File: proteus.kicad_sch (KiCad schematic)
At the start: 30 parts, among them J1 Conn_01x01, J13 Conn_01x03, J15 Sicma_56, J2 Conn_01x01, J3 Conn_01x01, J4 Conn_01x03, J5 Conn_01x05, J6 Conn_02x04_Counter_Clockwise, J9 Conn_01x04

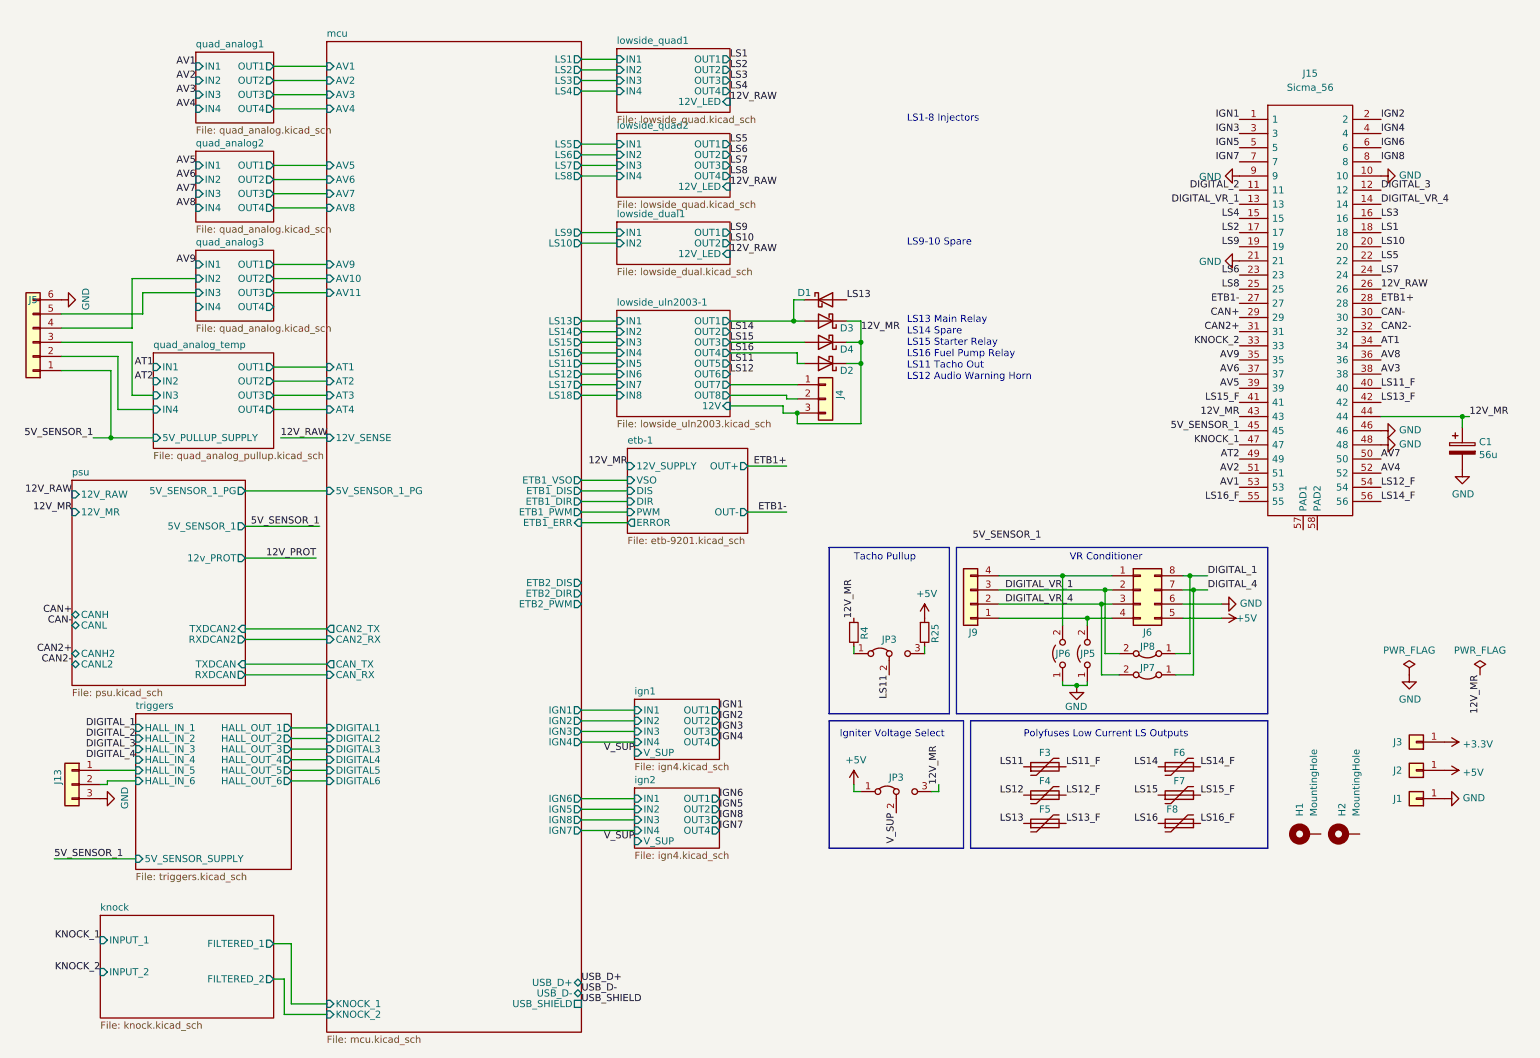
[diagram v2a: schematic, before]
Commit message: Add Stepper, fix Connector, add Testpoints, several changes
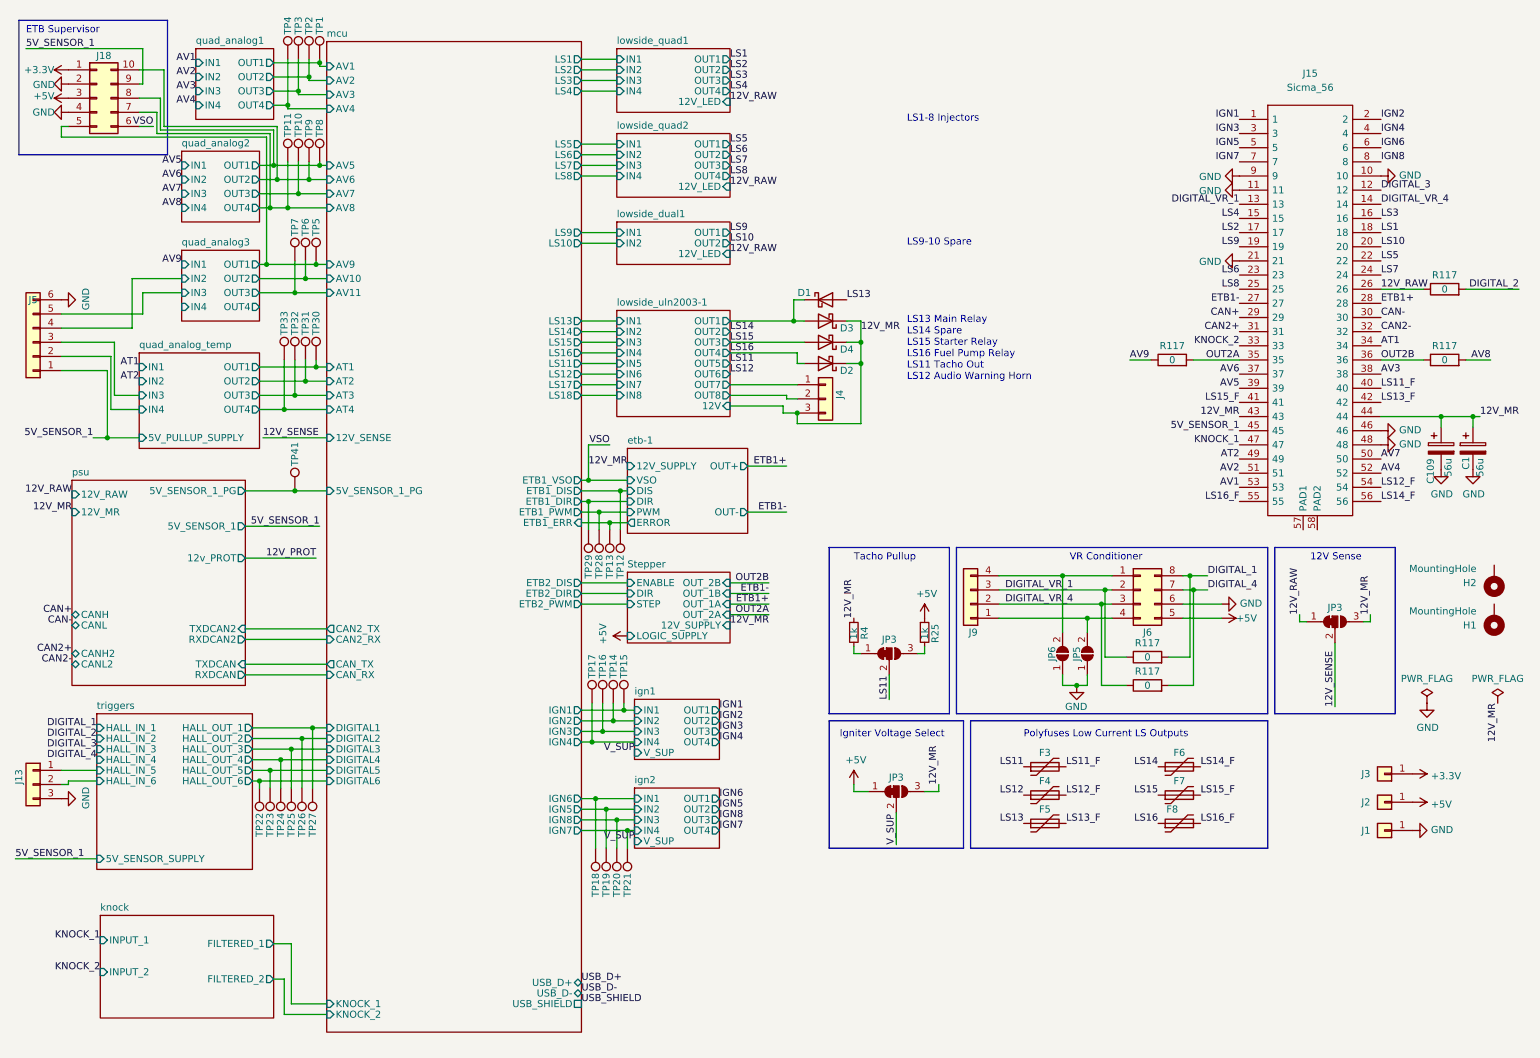
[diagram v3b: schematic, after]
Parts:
- removed JP7, JP8: Jumper_2_Bridged, Jumper:SolderJumper-2_P1.3mm_Bridged_RoundedPad1.0x1.5mm, symbol Jumper:Jumper_2_Bridged
- added C109: 56u, Capacitor_THT:CP_Radial_D8.0mm_P3.50mm, symbol proteus-rescue:CP-Device
- added J18: Conn_02x04_Counter_Clockwise, Connector_PinHeader_2.54mm:PinHeader_2x05_P2.54mm_Vertical, symbol Connector_Generic:Conn_02x05_Counter_Clockwise
- added JP3: Jumper_3_Bridged12, Jumper:SolderJumper-3_P1.3mm_Bridged12_RoundedPad1.0x1.5mm, symbol Jumper:SolderJumper_3_Bridged12
- added R117 (x5): 0, Resistor_SMD:R_0402_1005Metric, symbol Device:R
- added TP1, TP10, TP11, TP12, TP13, TP14, TP15, TP16, TP17, TP18, TP19, TP2, TP20, TP21, TP22, TP23, TP24, TP25, TP26, TP27, TP28, TP29, TP3, TP30, TP31, TP32, TP33, TP4, TP41, TP5, TP6, TP7, TP8, TP9: TestPoint, TestPoint:TestPoint_Pad_D1.0mm, symbol Connector:TestPoint
- D1, D2, D3, D4: LCSC C15874 -> C14996
- H1, H2, J1, J13, J15, J2, J3, J4, J5, J6, J9: now left out of the parts list
- JP3: symbol Jumper:Jumper_3_Bridged12 -> Jumper:SolderJumper_3_Bridged12; now left out of the parts list
- JP5, JP6: symbol Jumper:Jumper_2_Open -> Jumper:SolderJumper_2_Open; now left out of the parts list
- R25, R4: value R_Small -> 1k; footprint Resistor_SMD:R_0805_2012Metric -> Resistor_SMD:R_0402_1005Metric; LCSC (none) -> C106235
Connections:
- net +3V3: now also J18.1 (Pin_1)
- net +5V: now also J18.3 (Pin_3)
- net 12V_MR: now also C109.1, JP3.3 (B)
- net 12V_RAW: now also JP3.1 (A), R117.1
- net 5V_SENSOR_1: now also J18.9 (Pin_9)
- net AV8: now also R117.2; no longer J15.36
- net AV9: now also R117.1; no longer J15.35
- net DIGITAL_1: now also R117.2
- net DIGITAL_2: now also R117.2; no longer J15.11
- net DIGITAL_4: now also R117.2
- net DIGITAL_VR_1: now also R117.1
- net DIGITAL_VR_4: now also R117.1
- net GND: now also J15.11, C109.2, J18.2 (Pin_2), J18.4 (Pin_4)
- net etb-1/DIR: now also TP29.1
- net etb-1/DIS: now also TP12.1
- net etb-1/ERROR: now also TP13.1
- net etb-1/PWM: now also TP28.1
- net ign1/IN1: now also TP15.1
- net ign1/IN2: now also TP14.1
- net ign1/IN3: now also TP16.1
- net ign1/IN4: now also TP17.1
- net ign2/IN1: now also TP18.1
- net ign2/IN2: now also TP19.1
- net ign2/IN3: now also TP20.1
- net ign2/IN4: now also TP21.1
- net mcu/5V_SENSOR_1_PG: now also TP41.1
- net mcu/AT1: now also TP30.1
- net mcu/AT2: now also TP31.1
- net mcu/AT3: now also TP32.1
- net mcu/AT4: now also TP33.1
- net mcu/AV1: now also TP1.1
- net mcu/AV10: now also TP6.1
- net mcu/AV11: now also TP7.1
- net mcu/AV2: now also TP2.1
- net mcu/AV3: now also TP3.1
- net mcu/AV4: now also TP4.1
- net mcu/AV5: now also J18.8 (Pin_8), TP8.1
- net mcu/AV6: now also J18.10 (Pin_10), TP9.1
- net mcu/AV7: now also TP10.1
- net mcu/AV8: now also J18.7 (Pin_7), TP11.1
- net mcu/AV9: now also J18.5 (Pin_5), TP5.1
- net mcu/DIGITAL1: now also TP27.1
- net mcu/DIGITAL2: now also TP26.1
- net mcu/DIGITAL3: now also TP25.1
- net mcu/DIGITAL4: now also TP24.1
- net mcu/DIGITAL5: now also TP23.1
- net mcu/DIGITAL6: now also TP22.1
- new net 12V_SENSE: JP3.2 (C)
- new net OUT2A: J15.35, R117.2
- new net OUT2B: J15.36, R117.1
- new net VSO: J18.6 (Pin_6)
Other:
- added sheet Stepper (stepper.kicad_sch)
- note added: "12V Sense"
- note added: "ETB Supervisor"
- moved on the sheet: C1, H1, H2, J1, J13, J2, J3

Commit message: Production optimizations, voltage superv, etb sv conn
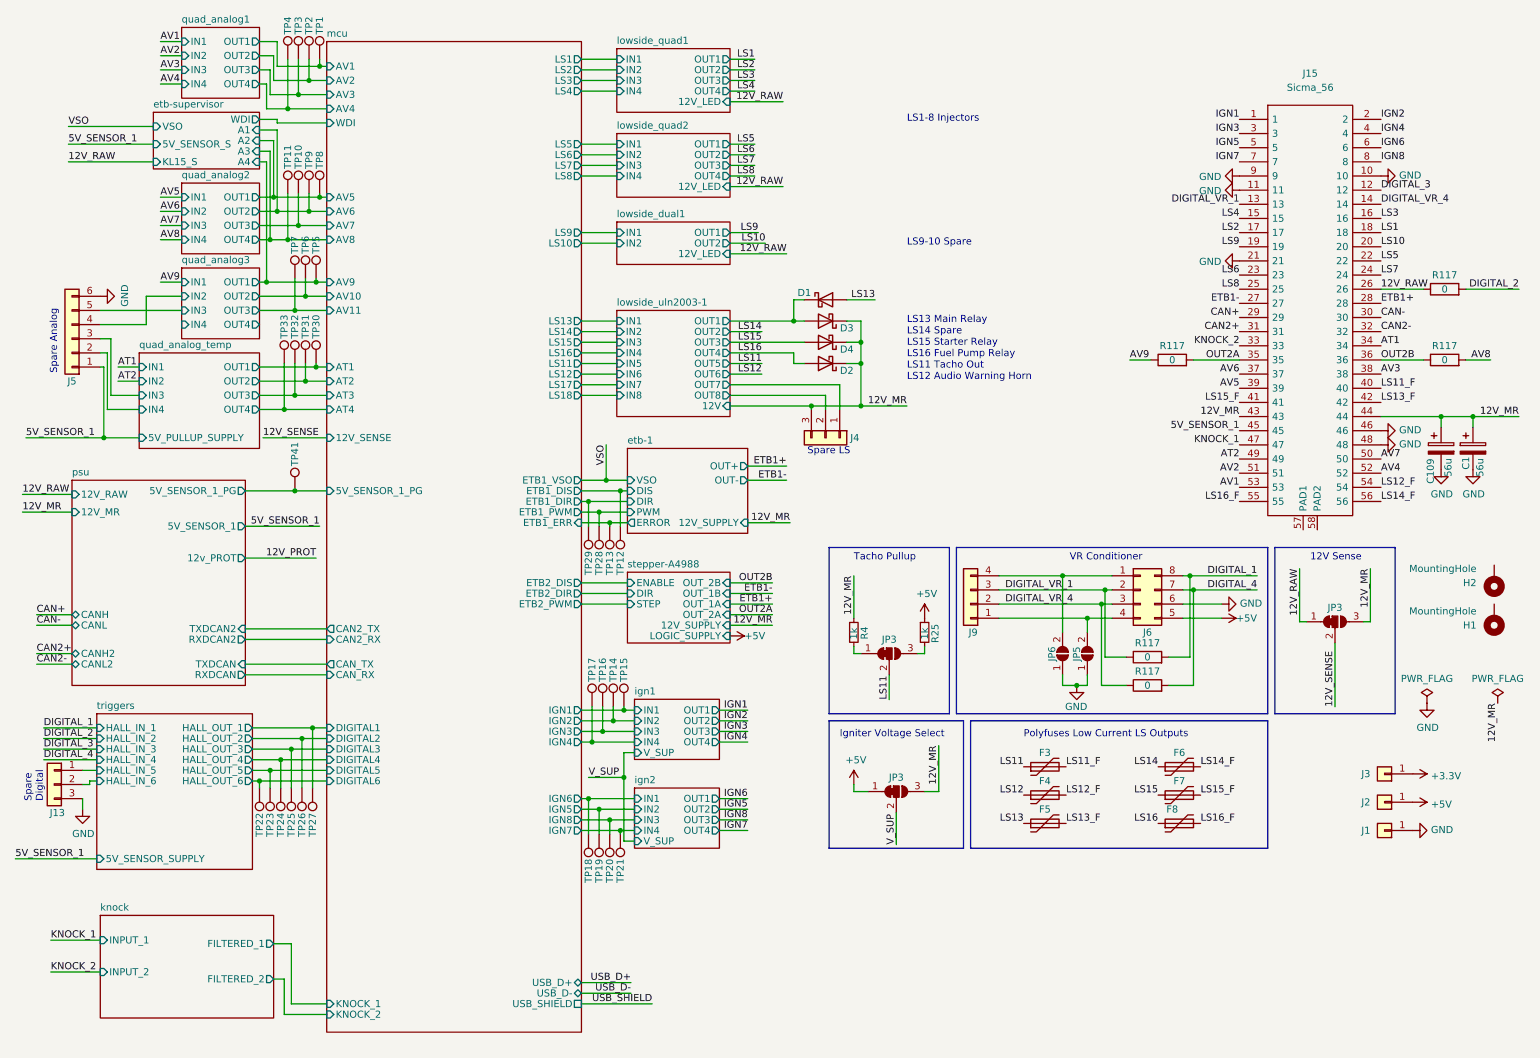
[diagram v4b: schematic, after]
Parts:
- removed J18: Conn_02x04_Counter_Clockwise, Connector_PinHeader_2.54mm:PinHeader_2x05_P2.54mm_Vertical, symbol Connector_Generic:Conn_02x05_Counter_Clockwise
- C1, C109: JLCPosOffset (none) -> 1.75,0
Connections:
- net mcu/AV5 renamed etb-supervisor/A2
- net mcu/AV6 renamed etb-supervisor/A1
- net mcu/AV8 renamed etb-supervisor/A3
- net mcu/AV9 renamed etb-supervisor/A4
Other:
- sheet Stepper renamed stepper-A4988
- added sheet etb-supervisor (etbsupervisor.kicad_sch)
- sheet mcu ports: added WDI; removed none
- note added: "Spare Analog"
- note added: "Spare Digital"
- note added: "Spare LS"
- note removed: "ETB Supervisor"
- moved on the sheet: J13, J4, J5, TP10, TP11, TP12, TP13, TP14, TP15, TP16, TP17, TP18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

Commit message: Optimize
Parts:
- R25, R4: LCSC C106235 -> C11702
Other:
- sheet etb-supervisor ports: added SRV05-4; removed none
- sheet mcu ports: added SRV05-4-IO2; removed none
- moved on the sheet: TP10, TP11, TP30, TP31, TP32, TP33, TP5, TP6, TP7, TP8, TP9
